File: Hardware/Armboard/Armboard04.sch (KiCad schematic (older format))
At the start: 24 parts

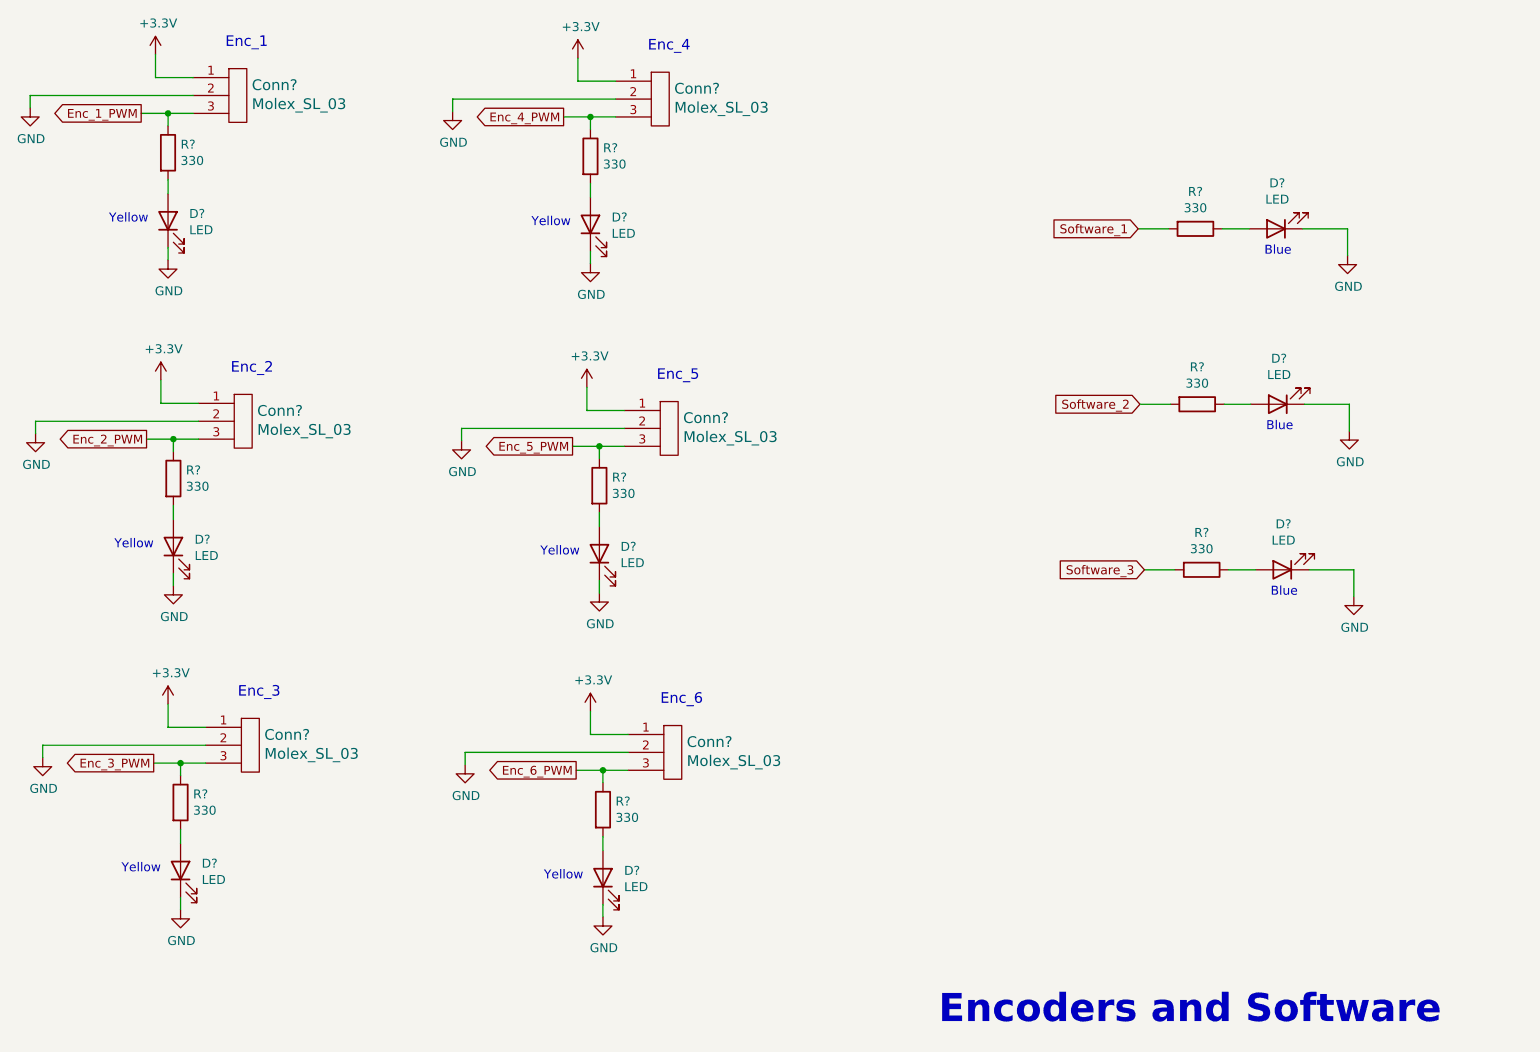
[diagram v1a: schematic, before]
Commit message: Assigned R/L/C footprints
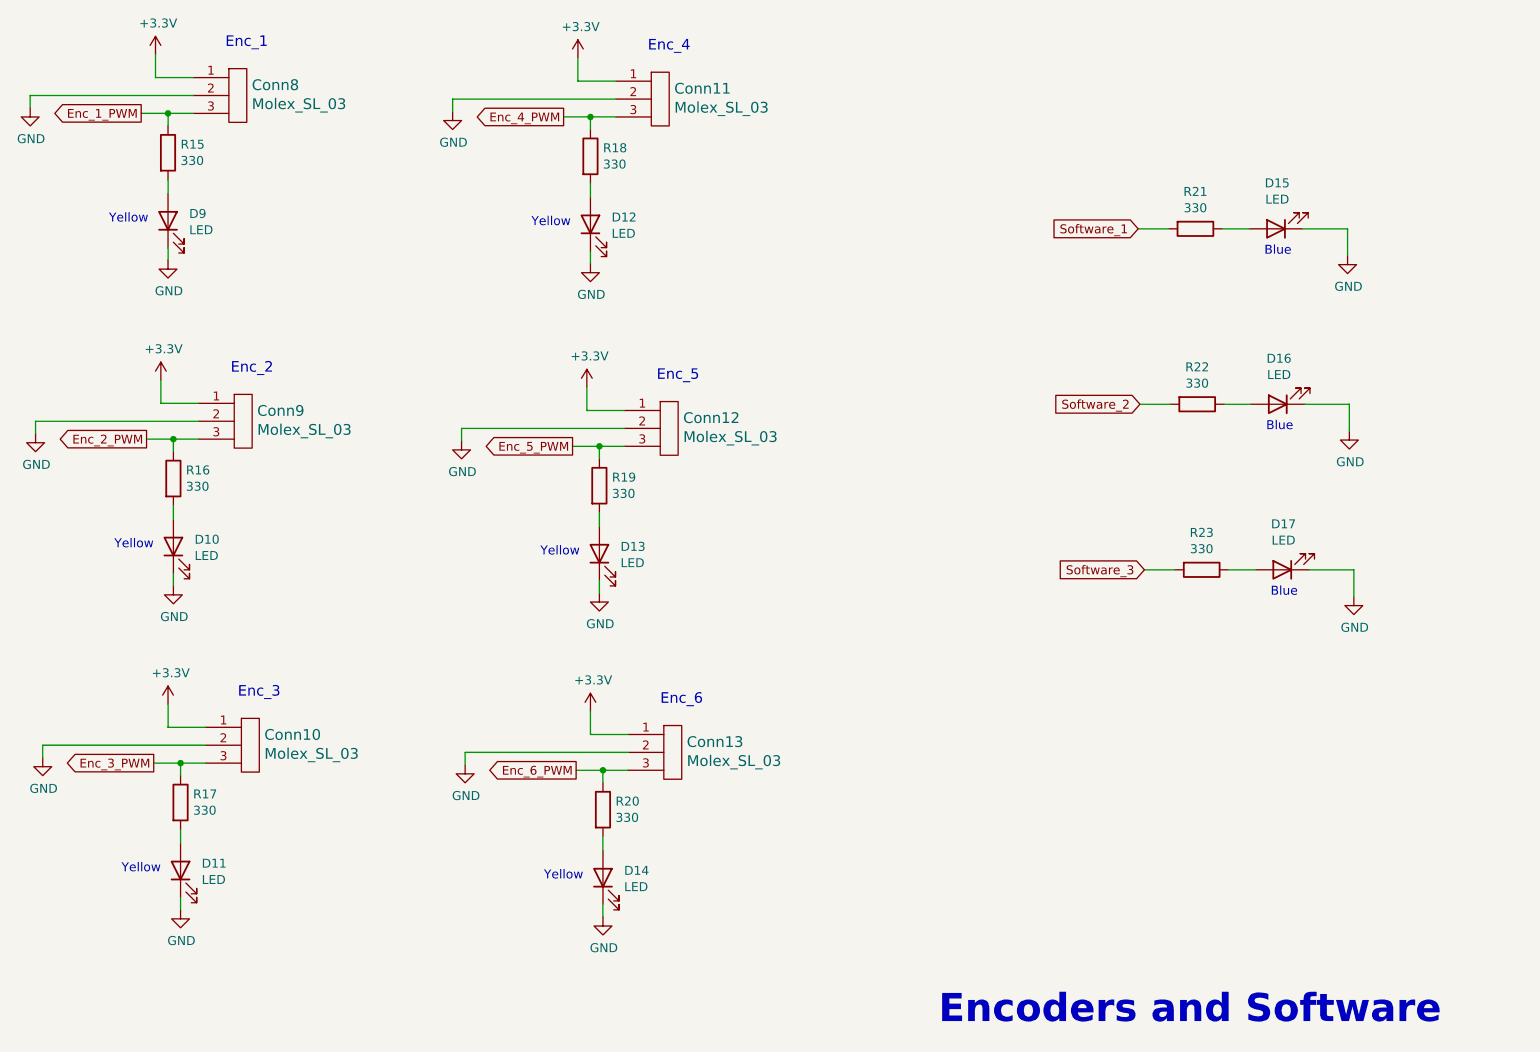
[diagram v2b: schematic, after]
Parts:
- R15, R16, R17, R18, R19, R20, R21, R22, R23: renamed from R?; footprint (none) -> Resistor_SMD:R_0603_1608Metric_Pad1.05x0.95mm_HandSolder
- gave numbers to parts that had none: 15

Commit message: Added more footprints
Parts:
- Conn10, Conn11, Conn12, Conn13, Conn8, Conn9: footprint (none) -> MRDT_Connectors:MOLEX_SL_03_Horizontal
- D10, D11, D12, D13, D14, D15, D16, D17, D9: footprint (none) -> LED_SMD:LED_0603_1608Metric_Pad1.05x0.95mm_HandSolder
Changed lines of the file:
@@
 F 0 "Conn9" H 2693 4128 60  0000 L CNN
 F 1 "Molex_SL_03" H 2693 4022 60  0000 L CNN
-F 2 "" H 2565 3920 60  0001 C CNN
+F 2 "MRDT_Connectors:MOLEX_SL_03_Horizontal" H 2565 3920 60  0001 C CNN
 F 3 "" H 2565 3920 60  0001 C CNN
 	1    2565 3920
@@
 F 0 "Conn10" H 2733 5938 60  0000 L CNN
 F 1 "Molex_SL_03" H 2733 5832 60  0000 L CNN
-F 2 "" H 2605 5730 60  0001 C CNN
+F 2 "MRDT_Connectors:MOLEX_SL_03_Horizontal" H 2605 5730 60  0001 C CNN
 F 3 "" H 2605 5730 60  0001 C CNN
 	1    2605 5730
@@
 F 0 "Conn11" H 5023 2328 60  0000 L CNN
 F 1 "Molex_SL_03" H 5023 2222 60  0000 L CNN
-F 2 "" H 4895 2120 60  0001 C CNN
+F 2 "MRDT_Connectors:MOLEX_SL_03_Horizontal" H 4895 2120 60  0001 C CNN
 F 3 "" H 4895 2120 60  0001 C CNN
 	1    4895 2120
@@
 F 0 "Conn12" H 5073 4168 60  0000 L CNN
 F 1 "Molex_SL_03" H 5073 4062 60  0000 L CNN
-F 2 "" H 4945 3960 60  0001 C CNN
+F 2 "MRDT_Connectors:MOLEX_SL_03_Horizontal" H 4945 3960 60  0001 C CNN
 F 3 "" H 4945 3960 60  0001 C CNN
 	1    4945 3960
@@
 F 0 "Conn13" H 5093 5978 60  0000 L CNN
 F 1 "Molex_SL_03" H 5093 5872 60  0000 L CNN
-F 2 "" H 4965 5770 60  0001 C CNN
+F 2 "MRDT_Connectors:MOLEX_SL_03_Horizontal" H 4965 5770 60  0001 C CNN
 F 3 "" H 4965 5770 60  0001 C CNN
 	1    4965 5770
@@
 F 0 "Conn8" H 2663 2308 60  0000 L CNN
 F 1 "Molex_SL_03" H 2663 2202 60  0000 L CNN
-F 2 "" H 2535 2100 60  0001 C CNN
+F 2 "MRDT_Connectors:MOLEX_SL_03_Horizontal" H 2535 2100 60  0001 C CNN
 F 3 "" H 2535 2100 60  0001 C CNN
 	1    2535 2100
@@
 F 0 "D9" V 2234 2532 50  0000 R CNN
 F 1 "LED" V 2143 2532 50  0000 R CNN
-F 2 "" H 2195 2650 50  0001 C CNN
+F 2 "LED_SMD:LED_0603_1608Metric_Pad1.05x0.95mm_HandSolder" H 2195 2650 50  0001 C CNN
 F 3 "~" H 2195 2650 50  0001 C CNN
 	1    2195 2650
@@
 F 0 "D10" V 2264 4352 50  0000 R CNN
 F 1 "LED" V 2173 4352 50  0000 R CNN
-F 2 "" H 2225 4470 50  0001 C CNN
+F 2 "LED_SMD:LED_0603_1608Metric_Pad1.05x0.95mm_HandSolder" H 2225 4470 50  0001 C CNN
 F 3 "~" H 2225 4470 50  0001 C CNN
 	1    2225 4470
@@
 F 0 "D11" V 2304 6162 50  0000 R CNN
 F 1 "LED" V 2213 6162 50  0000 R CNN
-F 2 "" H 2265 6280 50  0001 C CNN
+F 2 "LED_SMD:LED_0603_1608Metric_Pad1.05x0.95mm_HandSolder" H 2265 6280 50  0001 C CNN
 F 3 "~" H 2265 6280 50  0001 C CNN
 	1    2265 6280
@@
 F 0 "D12" V 4594 2552 50  0000 R CNN
 F 1 "LED" V 4503 2552 50  0000 R CNN
-F 2 "" H 4555 2670 50  0001 C CNN
+F 2 "LED_SMD:LED_0603_1608Metric_Pad1.05x0.95mm_HandSolder" H 4555 2670 50  0001 C CNN
 F 3 "~" H 4555 2670 50  0001 C CNN
 	1    4555 2670
@@
 F 0 "D13" V 4644 4392 50  0000 R CNN
 F 1 "LED" V 4553 4392 50  0000 R CNN
-F 2 "" H 4605 4510 50  0001 C CNN
+F 2 "LED_SMD:LED_0603_1608Metric_Pad1.05x0.95mm_HandSolder" H 4605 4510 50  0001 C CNN
 F 3 "~" H 4605 4510 50  0001 C CNN
 	1    4605 4510
@@
 F 0 "D14" V 4664 6202 50  0000 R CNN
 F 1 "LED" V 4573 6202 50  0000 R CNN
-F 2 "" H 4625 6320 50  0001 C CNN
+F 2 "LED_SMD:LED_0603_1608Metric_Pad1.05x0.95mm_HandSolder" H 4625 6320 50  0001 C CNN
 F 3 "~" H 4625 6320 50  0001 C CNN
 	1    4625 6320
@@
 F 0 "D15" H 8378 2440 50  0000 C CNN
 F 1 "LED" H 8378 2531 50  0000 C CNN
-F 2 "" H 8385 2695 50  0001 C CNN
+F 2 "LED_SMD:LED_0603_1608Metric_Pad1.05x0.95mm_HandSolder" H 8385 2695 50  0001 C CNN
 F 3 "~" H 8385 2695 50  0001 C CNN
 	1    8385 2695
@@
 F 0 "D16" H 8388 3420 50  0000 C CNN
 F 1 "LED" H 8388 3511 50  0000 C CNN
-F 2 "" H 8395 3675 50  0001 C CNN
+F 2 "LED_SMD:LED_0603_1608Metric_Pad1.05x0.95mm_HandSolder" H 8395 3675 50  0001 C CNN
 F 3 "~" H 8395 3675 50  0001 C CNN
 	1    8395 3675
@@
 F 0 "D17" H 8413 4345 50  0000 C CNN
 F 1 "LED" H 8413 4436 50  0000 C CNN
-F 2 "" H 8420 4600 50  0001 C CNN
+F 2 "LED_SMD:LED_0603_1608Metric_Pad1.05x0.95mm_HandSolder" H 8420 4600 50  0001 C CNN
 F 3 "~" H 8420 4600 50  0001 C CNN
 	1    8420 4600

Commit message: Imported footprints to layout
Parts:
- Conn10, Conn11, Conn12, Conn13, Conn8, Conn9: footprint MRDT_Connectors:MOLEX_SL_03_Horizontal -> MRDT_Connectors:MOLEX_SL_03_Vertical
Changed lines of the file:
@@
 F 0 "Conn9" H 2693 4128 60  0000 L CNN
 F 1 "Molex_SL_03" H 2693 4022 60  0000 L CNN
-F 2 "MRDT_Connectors:MOLEX_SL_03_Horizontal" H 2565 3920 60  0001 C CNN
+F 2 "MRDT_Connectors:MOLEX_SL_03_Vertical" H 2565 3920 60  0001 C CNN
 F 3 "" H 2565 3920 60  0001 C CNN
 	1    2565 3920
@@
 F 0 "Conn10" H 2733 5938 60  0000 L CNN
 F 1 "Molex_SL_03" H 2733 5832 60  0000 L CNN
-F 2 "MRDT_Connectors:MOLEX_SL_03_Horizontal" H 2605 5730 60  0001 C CNN
+F 2 "MRDT_Connectors:MOLEX_SL_03_Vertical" H 2605 5730 60  0001 C CNN
 F 3 "" H 2605 5730 60  0001 C CNN
 	1    2605 5730
@@
 F 0 "Conn11" H 5023 2328 60  0000 L CNN
 F 1 "Molex_SL_03" H 5023 2222 60  0000 L CNN
-F 2 "MRDT_Connectors:MOLEX_SL_03_Horizontal" H 4895 2120 60  0001 C CNN
+F 2 "MRDT_Connectors:MOLEX_SL_03_Vertical" H 4895 2120 60  0001 C CNN
 F 3 "" H 4895 2120 60  0001 C CNN
 	1    4895 2120
@@
 F 0 "Conn12" H 5073 4168 60  0000 L CNN
 F 1 "Molex_SL_03" H 5073 4062 60  0000 L CNN
-F 2 "MRDT_Connectors:MOLEX_SL_03_Horizontal" H 4945 3960 60  0001 C CNN
+F 2 "MRDT_Connectors:MOLEX_SL_03_Vertical" H 4945 3960 60  0001 C CNN
 F 3 "" H 4945 3960 60  0001 C CNN
 	1    4945 3960
@@
 F 0 "Conn13" H 5093 5978 60  0000 L CNN
 F 1 "Molex_SL_03" H 5093 5872 60  0000 L CNN
-F 2 "MRDT_Connectors:MOLEX_SL_03_Horizontal" H 4965 5770 60  0001 C CNN
+F 2 "MRDT_Connectors:MOLEX_SL_03_Vertical" H 4965 5770 60  0001 C CNN
 F 3 "" H 4965 5770 60  0001 C CNN
 	1    4965 5770
@@
 F 0 "Conn8" H 2663 2308 60  0000 L CNN
 F 1 "Molex_SL_03" H 2663 2202 60  0000 L CNN
-F 2 "MRDT_Connectors:MOLEX_SL_03_Horizontal" H 2535 2100 60  0001 C CNN
+F 2 "MRDT_Connectors:MOLEX_SL_03_Vertical" H 2535 2100 60  0001 C CNN
 F 3 "" H 2535 2100 60  0001 C CNN
 	1    2535 2100

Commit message: Fixed some library issues and moved Gerbs to Manufacturing folder
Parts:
- Conn10, Conn11, Conn12, Conn13, Conn8, Conn9: symbol Armboard-rescue:Molex_SL_03-MRDT_Connectors-Armboard-rescue -> MRDT_Connectors:Molex_SL_03
- D10, D11, D12, D13, D14, D15, D16, D17, D9: footprint LED_SMD:LED_0603_1608Metric_Pad1.05x0.95mm_HandSolder -> Diode_SMD:D_0603_1608Metric_Pad1.05x0.95mm_HandSolder
- R15, R16, R17, R18, R19, R20, R21, R22, R23: footprint Resistor_SMD:R_0603_1608Metric_Pad1.05x0.95mm_HandSolder -> Resistor_SMD:R_0603_1608Metric_Pad0.98x0.95mm_HandSolder
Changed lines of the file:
@@
 EESchema Schematic File Version 4
+LIBS:Armboard-cache
 EELAYER 30 0
 EELAYER END
@@
 $EndDescr
 $Comp
-L Armboard-rescue:Molex_SL_03-MRDT_Connectors-Armboard-rescue Conn9
+L MRDT_Connectors:Molex_SL_03 Conn9
 U 1 1 5F78F4A7
 P 2565 3920
@@
 Enc_2
 $Comp
-L Armboard-rescue:Molex_SL_03-MRDT_Connectors-Armboard-rescue Conn10
+L MRDT_Connectors:Molex_SL_03 Conn10
 U 1 1 5F78F9EB
 P 2605 5730
@@
 Enc_3
 $Comp
-L Armboard-rescue:Molex_SL_03-MRDT_Connectors-Armboard-rescue Conn11
+L MRDT_Connectors:Molex_SL_03 Conn11
 U 1 1 5F793695
 P 4895 2120
@@
 Enc_4
 $Comp
-L Armboard-rescue:Molex_SL_03-MRDT_Connectors-Armboard-rescue Conn12
+L MRDT_Connectors:Molex_SL_03 Conn12
 U 1 1 5F7936AB
 P 4945 3960
@@
 Enc_5
 $Comp
-L Armboard-rescue:Molex_SL_03-MRDT_Connectors-Armboard-rescue Conn13
+L MRDT_Connectors:Molex_SL_03 Conn13
 U 1 1 5F7936C1
 P 4965 5770
@@
 Encoders and Software
 $Comp
-L Armboard-rescue:Molex_SL_03-MRDT_Connectors-Armboard-rescue Conn8
+L MRDT_Connectors:Molex_SL_03 Conn8
 U 1 1 5F845537
 P 2535 2100
@@
 F 0 "R15" H 2265 2316 50  0000 L CNN
 F 1 "330" H 2265 2225 50  0000 L CNN
-F 2 "Resistor_SMD:R_0603_1608Metric_Pad1.05x0.95mm_HandSolder" V 2125 2270 50  0001 C CNN
+F 2 "Resistor_SMD:R_0603_1608Metric_Pad0.98x0.95mm_HandSolder" V 2125 2270 50  0001 C CNN
 F 3 "~" H 2195 2270 50  0001 C CNN
 	1    2195 2270
@@
 F 0 "D9" V 2234 2532 50  0000 R CNN
 F 1 "LED" V 2143 2532 50  0000 R CNN
-F 2 "LED_SMD:LED_0603_1608Metric_Pad1.05x0.95mm_HandSolder" H 2195 2650 50  0001 C CNN
+F 2 "Diode_SMD:D_0603_1608Metric_Pad1.05x0.95mm_HandSolder" H 2195 2650 50  0001 C CNN
 F 3 "~" H 2195 2650 50  0001 C CNN
 	1    2195 2650
@@
 F 0 "R16" H 2295 4136 50  0000 L CNN
 F 1 "330" H 2295 4045 50  0000 L CNN
-F 2 "Resistor_SMD:R_0603_1608Metric_Pad1.05x0.95mm_HandSolder" V 2155 4090 50  0001 C CNN
+F 2 "Resistor_SMD:R_0603_1608Metric_Pad0.98x0.95mm_HandSolder" V 2155 4090 50  0001 C CNN
 F 3 "~" H 2225 4090 50  0001 C CNN
 	1    2225 4090
@@
 F 0 "D10" V 2264 4352 50  0000 R CNN
 F 1 "LED" V 2173 4352 50  0000 R CNN
-F 2 "LED_SMD:LED_0603_1608Metric_Pad1.05x0.95mm_HandSolder" H 2225 4470 50  0001 C CNN
+F 2 "Diode_SMD:D_0603_1608Metric_Pad1.05x0.95mm_HandSolder" H 2225 4470 50  0001 C CNN
 F 3 "~" H 2225 4470 50  0001 C CNN
 	1    2225 4470
@@
 F 0 "R17" H 2335 5946 50  0000 L CNN
 F 1 "330" H 2335 5855 50  0000 L CNN
-F 2 "Resistor_SMD:R_0603_1608Metric_Pad1.05x0.95mm_HandSolder" V 2195 5900 50  0001 C CNN
+F 2 "Resistor_SMD:R_0603_1608Metric_Pad0.98x0.95mm_HandSolder" V 2195 5900 50  0001 C CNN
 F 3 "~" H 2265 5900 50  0001 C CNN
 	1    2265 5900
@@
 F 0 "D11" V 2304 6162 50  0000 R CNN
 F 1 "LED" V 2213 6162 50  0000 R CNN
-F 2 "LED_SMD:LED_0603_1608Metric_Pad1.05x0.95mm_HandSolder" H 2265 6280 50  0001 C CNN
+F 2 "Diode_SMD:D_0603_1608Metric_Pad1.05x0.95mm_HandSolder" H 2265 6280 50  0001 C CNN
 F 3 "~" H 2265 6280 50  0001 C CNN
 	1    2265 6280
@@
 F 0 "R18" H 4625 2336 50  0000 L CNN
 F 1 "330" H 4625 2245 50  0000 L CNN
-F 2 "Resistor_SMD:R_0603_1608Metric_Pad1.05x0.95mm_HandSolder" V 4485 2290 50  0001 C CNN
+F 2 "Resistor_SMD:R_0603_1608Metric_Pad0.98x0.95mm_HandSolder" V 4485 2290 50  0001 C CNN
 F 3 "~" H 4555 2290 50  0001 C CNN
 	1    4555 2290
@@
 F 0 "D12" V 4594 2552 50  0000 R CNN
 F 1 "LED" V 4503 2552 50  0000 R CNN
-F 2 "LED_SMD:LED_0603_1608Metric_Pad1.05x0.95mm_HandSolder" H 4555 2670 50  0001 C CNN
+F 2 "Diode_SMD:D_0603_1608Metric_Pad1.05x0.95mm_HandSolder" H 4555 2670 50  0001 C CNN
 F 3 "~" H 4555 2670 50  0001 C CNN
 	1    4555 2670
@@
 F 0 "R19" H 4675 4176 50  0000 L CNN
 F 1 "330" H 4675 4085 50  0000 L CNN
-F 2 "Resistor_SMD:R_0603_1608Metric_Pad1.05x0.95mm_HandSolder" V 4535 4130 50  0001 C CNN
+F 2 "Resistor_SMD:R_0603_1608Metric_Pad0.98x0.95mm_HandSolder" V 4535 4130 50  0001 C CNN
 F 3 "~" H 4605 4130 50  0001 C CNN
 	1    4605 4130
@@
 F 0 "D13" V 4644 4392 50  0000 R CNN
 F 1 "LED" V 4553 4392 50  0000 R CNN
-F 2 "LED_SMD:LED_0603_1608Metric_Pad1.05x0.95mm_HandSolder" H 4605 4510 50  0001 C CNN
+F 2 "Diode_SMD:D_0603_1608Metric_Pad1.05x0.95mm_HandSolder" H 4605 4510 50  0001 C CNN
 F 3 "~" H 4605 4510 50  0001 C CNN
 	1    4605 4510
@@
 F 0 "R20" H 4695 5986 50  0000 L CNN
 F 1 "330" H 4695 5895 50  0000 L CNN
-F 2 "Resistor_SMD:R_0603_1608Metric_Pad1.05x0.95mm_HandSolder" V 4555 5940 50  0001 C CNN
+F 2 "Resistor_SMD:R_0603_1608Metric_Pad0.98x0.95mm_HandSolder" V 4555 5940 50  0001 C CNN
 F 3 "~" H 4625 5940 50  0001 C CNN
 	1    4625 5940
@@
 F 0 "D14" V 4664 6202 50  0000 R CNN
 F 1 "LED" V 4573 6202 50  0000 R CNN
-F 2 "LED_SMD:LED_0603_1608Metric_Pad1.05x0.95mm_HandSolder" H 4625 6320 50  0001 C CNN
+F 2 "Diode_SMD:D_0603_1608Metric_Pad1.05x0.95mm_HandSolder" H 4625 6320 50  0001 C CNN
 F 3 "~" H 4625 6320 50  0001 C CNN
 	1    4625 6320
@@
 F 0 "R21" V 7728 2695 50  0000 C CNN
 F 1 "330" V 7819 2695 50  0000 C CNN
-F 2 "Resistor_SMD:R_0603_1608Metric_Pad1.05x0.95mm_HandSolder" V 7865 2695 50  0001 C CNN
+F 2 "Resistor_SMD:R_0603_1608Metric_Pad0.98x0.95mm_HandSolder" V 7865 2695 50  0001 C CNN
 F 3 "~" H 7935 2695 50  0001 C CNN
 	1    7935 2695
@@
 F 0 "D15" H 8378 2440 50  0000 C CNN
 F 1 "LED" H 8378 2531 50  0000 C CNN
-F 2 "LED_SMD:LED_0603_1608Metric_Pad1.05x0.95mm_HandSolder" H 8385 2695 50  0001 C CNN
+F 2 "Diode_SMD:D_0603_1608Metric_Pad1.05x0.95mm_HandSolder" H 8385 2695 50  0001 C CNN
 F 3 "~" H 8385 2695 50  0001 C CNN
 	1    8385 2695
@@
 F 0 "R22" V 7738 3675 50  0000 C CNN
 F 1 "330" V 7829 3675 50  0000 C CNN
-F 2 "Resistor_SMD:R_0603_1608Metric_Pad1.05x0.95mm_HandSolder" V 7875 3675 50  0001 C CNN
+F 2 "Resistor_SMD:R_0603_1608Metric_Pad0.98x0.95mm_HandSolder" V 7875 3675 50  0001 C CNN
 F 3 "~" H 7945 3675 50  0001 C CNN
 	1    7945 3675
@@
 F 0 "D16" H 8388 3420 50  0000 C CNN
 F 1 "LED" H 8388 3511 50  0000 C CNN
-F 2 "LED_SMD:LED_0603_1608Metric_Pad1.05x0.95mm_HandSolder" H 8395 3675 50  0001 C CNN
+F 2 "Diode_SMD:D_0603_1608Metric_Pad1.05x0.95mm_HandSolder" H 8395 3675 50  0001 C CNN
 F 3 "~" H 8395 3675 50  0001 C CNN
 	1    8395 3675
@@
 F 0 "R23" V 7763 4600 50  0000 C CNN
 F 1 "330" V 7854 4600 50  0000 C CNN
-F 2 "Resistor_SMD:R_0603_1608Metric_Pad1.05x0.95mm_HandSolder" V 7900 4600 50  0001 C CNN
+F 2 "Resistor_SMD:R_0603_1608Metric_Pad0.98x0.95mm_HandSolder" V 7900 4600 50  0001 C CNN
 F 3 "~" H 7970 4600 50  0001 C CNN
 	1    7970 4600
@@
 F 0 "D17" H 8413 4345 50  0000 C CNN
 F 1 "LED" H 8413 4436 50  0000 C CNN
-F 2 "LED_SMD:LED_0603_1608Metric_Pad1.05x0.95mm_HandSolder" H 8420 4600 50  0001 C CNN
+F 2 "Diode_SMD:D_0603_1608Metric_Pad1.05x0.95mm_HandSolder" H 8420 4600 50  0001 C CNN
 F 3 "~" H 8420 4600 50  0001 C CNN
 	1    8420 4600
